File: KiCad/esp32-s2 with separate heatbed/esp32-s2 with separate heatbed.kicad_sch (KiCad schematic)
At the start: 54 parts, among them IC1 ESP32-S2FN4R2, J1 PJ-037B, J2 USB_C_Receptacle_USB2.0, J3 TB003-500-P02BE, J4 TB003-500-P02BE, J5 Conn_01x03_Male, Q1 PJD25N06A_L2_00001, U1 LD1117S33TR_SOT223, U2 MAX31855KASA, Y1 ECS-400-15-33B-CTN-TR

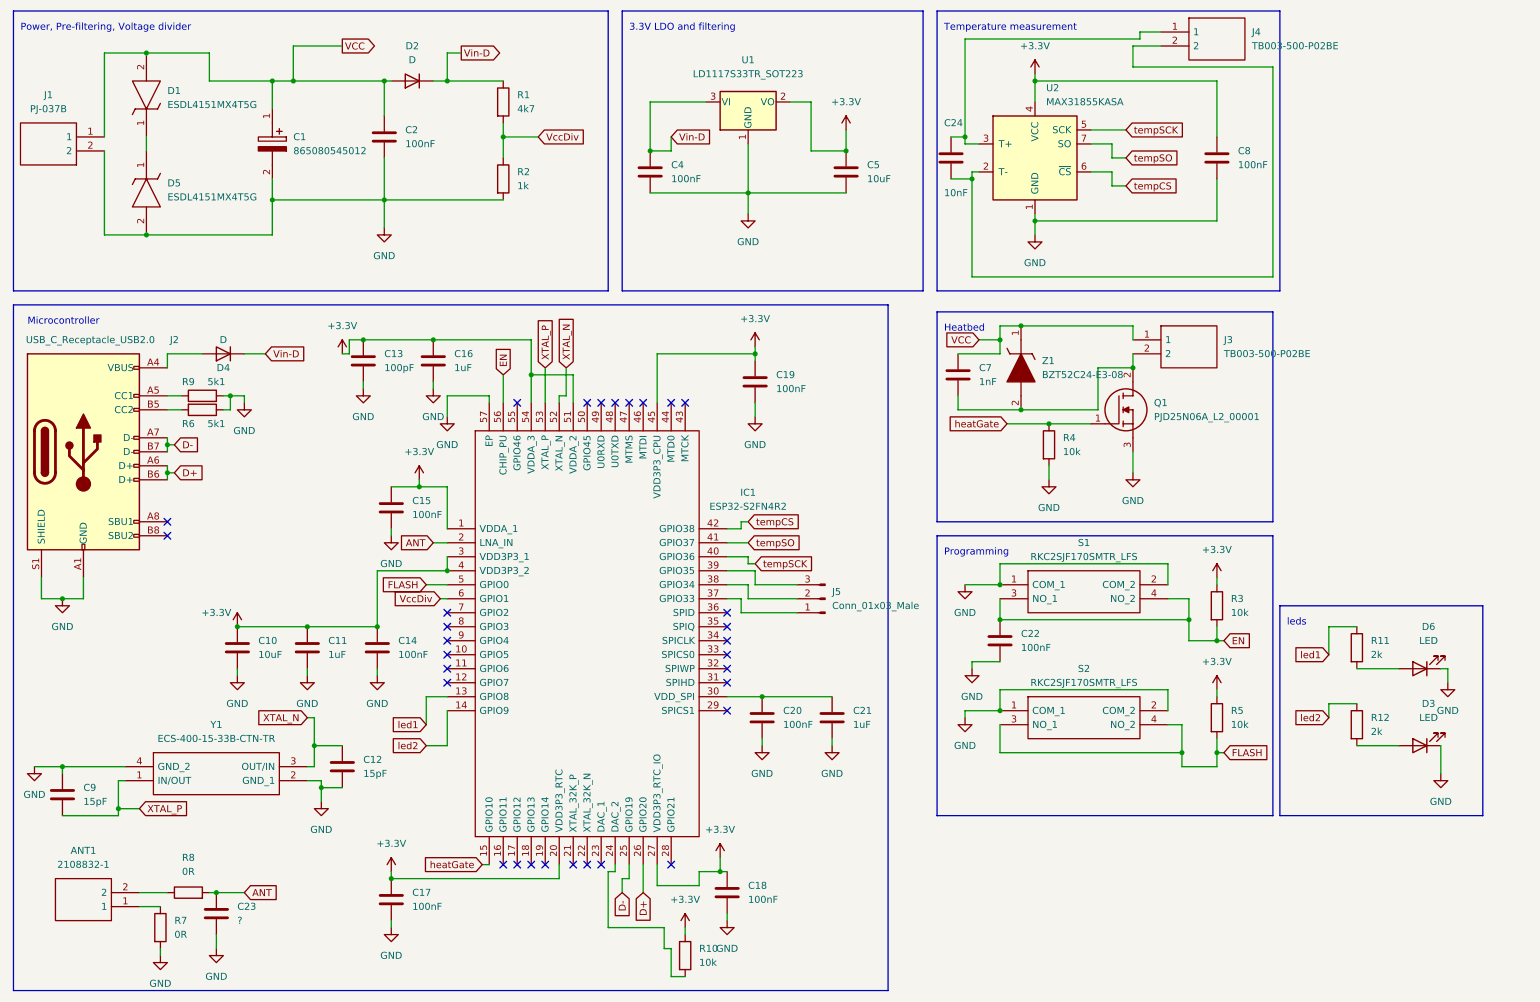
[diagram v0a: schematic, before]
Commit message: Set value for D2/D4 and add note about C23 and LED resistors
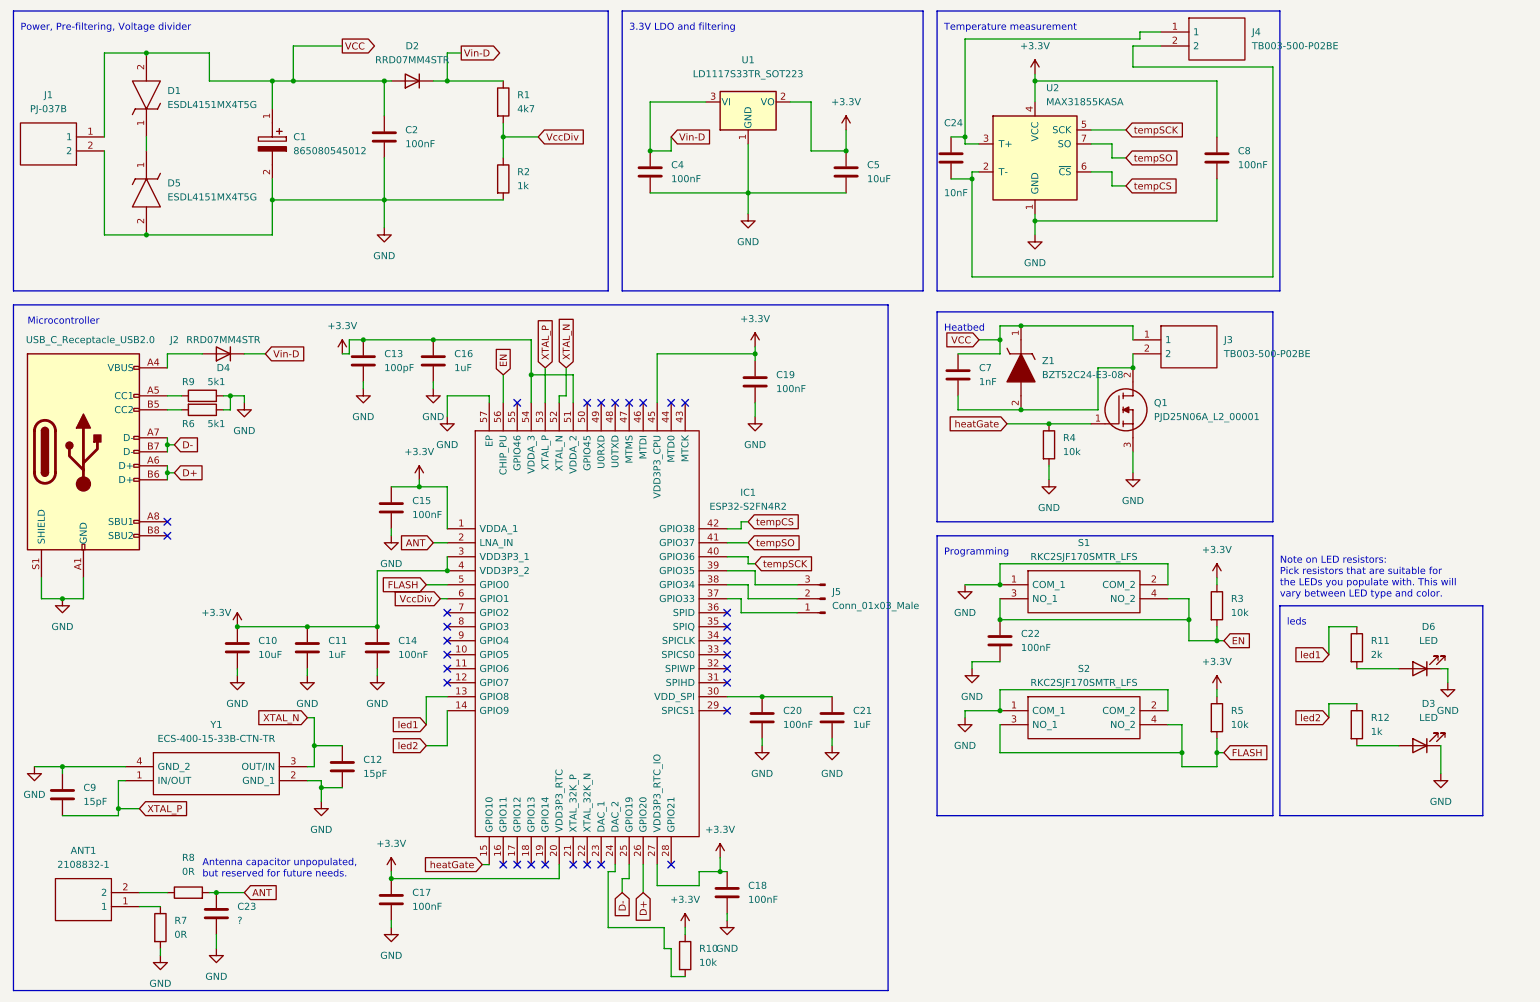
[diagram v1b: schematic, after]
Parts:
- D2, D4: value D -> RRD07MM4STR
- R12: value 2k -> 1k
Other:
- note added: "Antenna capacitor unpopulated, but reserved for future needs."
- note added: "Note on LED resistors: Pick resistors that are suitable for the LEDs you populate with. This will vary between LED type and color."
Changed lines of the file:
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@@
     (stroke (width 0) (type default) (color 0 0 0 0))
+  )
+  (text "Antenna capacitor unpopulated,\nbut reserved for future needs."
+    (at 50.8 172.72 0)
+    (effects (font (size 1.27 1.27)) (justify left bottom))
   )
   (text "Heatbed" (at 185.42 73.66 0)
@@
   )
   (text "Power, Pre-filtering, Voltage divider" (at 17.78 19.05 0)
+    (effects (font (size 1.27 1.27)) (justify left bottom))
+  )
+  (text "Note on LED resistors:\nPick resistors that are suitable for\nthe LEDs you populate with. This will\nvary between LED type and color."
+    (at 246.38 121.92 0)
     (effects (font (size 1.27 1.27)) (justify left bottom))
   )
@@
       (effects (font (size 1.27 1.27)) (justify left))
     )
-    (property "Value" "2k" (id 1) (at 262.89 146.0499 0)
+    (property "Value" "1k" (id 1) (at 262.89 146.0499 0)
       (effects (font (size 1.27 1.27)) (justify left))
     )
@@
     (in_bom yes) (on_board yes) (fields_autoplaced)
     (property "Reference" "D2" (id 0) (at 88.9 21.59 0))
-    (property "Value" "D" (id 1) (at 88.9 24.13 0))
+    (property "Value" "RRD07MM4STR" (id 1) (at 88.9 24.13 0))
     (property "Footprint" "Diode_SMD:D_SOD-123" (id 2) (at 88.9 27.94 0)
       (effects (font (size 1.27 1.27)) hide)
@@
     (in_bom yes) (on_board yes)
     (property "Reference" "D4" (id 0) (at 54.61 80.01 0))
-    (property "Value" "D" (id 1) (at 54.61 74.93 0))
+    (property "Value" "RRD07MM4STR" (id 1) (at 54.61 74.93 0))
     (property "Footprint" "Diode_SMD:D_SOD-123" (id 2) (at 54.61 77.47 0)
       (effects (font (size 1.27 1.27)) hide)
@@
     )
     (path "/74383a9a-9fb0-4eb2-95d8-0d39d92a7c66"
-      (reference "D2") (unit 1) (value "D") (footprint "Diode_SMD:D_SOD-123")
+      (reference "D2") (unit 1) (value "RRD07MM4STR") (footprint "Diode_SMD:D_SOD-123")
     )
     (path "/148fbc61-4d06-44c5-8be4-1aeaa9f99fc0"
@@
     )
     (path "/7c9c17f7-2c1d-4e33-a4f0-562d9266a71f"
-      (reference "D4") (unit 1) (value "D") (footprint "Diode_SMD:D_SOD-123")
+      (reference "D4") (unit 1) (value "RRD07MM4STR") (footprint "Diode_SMD:D_SOD-123")
     )
     (path "/40cb2244-aa79-463e-9505-e1e627ad26d1"
@@
     )
     (path "/11d89545-ac37-4cf8-94b0-02ca18d65b9a"
-      (reference "R12") (unit 1) (value "2k") (footprint "Resistor_SMD:R_0603_1608Metric")
+      (reference "R12") (unit 1) (value "1k") (footprint "Resistor_SMD:R_0603_1608Metric")
     )
     (path "/7457f92b-d768-49d2-a7c7-6385146769b6"
